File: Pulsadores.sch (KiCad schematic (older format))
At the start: 13 parts, among them SW1 Izquierda, SW2 Arriba, SW3 Abajo, SW4 Derecha, U6 74HC148

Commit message: añaadido zocalo para sensor de temperatura y primera distribucion sobre la PCB
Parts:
- added C7: 100n, Capacitors_SMD:C_0805, symbol C
- R21, R22, R23, R24, R25, R26, R27, R28: footprint (none) -> Resistors_SMD:R_0805
- SW1, SW2, SW3, SW4: footprint (none) -> Relays_and_Contacts:CANAL_ELECTRONIC_DTSM-31N-B
- U6: footprint (none) -> Housings_SOIC:SOIC-16_3.9x9.9mm_Pitch1.27mm
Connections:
- net +5V: now also C7.1
- net GND: now also C7.2
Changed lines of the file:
@@
 $Descr User 8268 5846
 encoding utf-8
-Sheet 9 13
+Sheet 9 14
 Title ""
 Date ""
@@
 F 0 "U6" H 5650 3075 50  0000 C CNN
 F 1 "74HC148" H 5650 2984 50  0000 C CNN
-F 2 "" H 5650 2450 50  0000 C CNN
+F 2 "Housings_SOIC:SOIC-16_3.9x9.9mm_Pitch1.27mm" H 5650 2450 50  0001 C CNN
 F 3 "http://www.tme.eu/es/Document/f2fc394d57399d0b6e6c6b1f0163be7e/SN74HC148N.pdf" H 5650 2450 50  0001 C CNN
 F 4 "Texas Instruments" H 5650 2450 60  0001 C CNN "Fabricante"
@@
 F 0 "SW2" H 2400 2305 50  0000 C CNN
 F 1 "Arriba" H 2400 2214 50  0000 C CNN
-F 2 "" H 2400 2050 50  0000 C CNN
+F 2 "Relays_and_Contacts:CANAL_ELECTRONIC_DTSM-31N-B" H 2400 2050 50  0001 C CNN
 F 3 "" H 2400 2050 50  0000 C CNN
 	1    2400 2050
@@
 F 0 "SW3" H 2400 3355 50  0000 C CNN
 F 1 "Abajo" H 2400 3264 50  0000 C CNN
-F 2 "" H 2400 3100 50  0000 C CNN
+F 2 "Relays_and_Contacts:CANAL_ELECTRONIC_DTSM-31N-B" H 2400 3100 50  0001 C CNN
 F 3 "" H 2400 3100 50  0000 C CNN
 	1    2400 3100
@@
 F 0 "SW4" H 3250 2855 50  0000 C CNN
 F 1 "Derecha" H 3250 2764 50  0000 C CNN
-F 2 "" H 3250 2600 50  0000 C CNN
+F 2 "Relays_and_Contacts:CANAL_ELECTRONIC_DTSM-31N-B" H 3250 2600 50  0001 C CNN
 F 3 "" H 3250 2600 50  0000 C CNN
 	1    3250 2600
@@
 F 0 "SW1" H 1450 2855 50  0000 C CNN
 F 1 "Izquierda" H 1450 2764 50  0000 C CNN
-F 2 "" H 1450 2600 50  0000 C CNN
+F 2 "Relays_and_Contacts:CANAL_ELECTRONIC_DTSM-31N-B" H 1450 2600 50  0001 C CNN
 F 3 "" H 1450 2600 50  0000 C CNN
 	1    1450 2600
@@
 $EndComp
 Wire Wire Line
-	2700 2050 3950 2050
-Wire Wire Line
-	3950 2050 5050 2050
-Wire Wire Line
-	2700 2150 4200 2150
-Wire Wire Line
-	4200 2150 5050 2150
+	2700 2050 5050 2050
+Wire Wire Line
+	2700 2150 5050 2150
 Wire Wire Line
 	2700 2150 2700 2600
@@
 	3650 2600 3650 2250
 Wire Wire Line
-	3650 2250 4450 2250
-Wire Wire Line
-	4450 2250 5050 2250
-Wire Wire Line
-	3750 2350 4700 2350
-Wire Wire Line
-	4700 2350 5050 2350
+	3650 2250 5050 2250
+Wire Wire Line
+	3750 2350 5050 2350
 Wire Wire Line
 	3750 3100 3750 2350
@@
 F 0 "R21" H 4020 1696 50  0000 L CNN
 F 1 "10K" V 3950 1550 50  0000 L CNN
-F 2 "" V 3880 1650 50  0000 C CNN
+F 2 "Resistors_SMD:R_0805" V 3880 1650 50  0001 C CNN
 F 3 "" H 3950 1650 50  0000 C CNN
 F 4 "~" H 3950 1650 60  0001 C CNN "Fabricante"
@@
 F 0 "R23" H 4270 1696 50  0000 L CNN
 F 1 "10K" V 4200 1550 50  0000 L CNN
-F 2 "" V 4130 1650 50  0000 C CNN
+F 2 "Resistors_SMD:R_0805" V 4130 1650 50  0001 C CNN
 F 3 "" H 4200 1650 50  0000 C CNN
 F 4 "~" H 4200 1650 60  0001 C CNN "Fabricante"
@@
 F 0 "R25" H 4520 1696 50  0000 L CNN
 F 1 "10K" V 4450 1550 50  0000 L CNN
-F 2 "" V 4380 1650 50  0000 C CNN
+F 2 "Resistors_SMD:R_0805" V 4380 1650 50  0001 C CNN
 F 3 "" H 4450 1650 50  0000 C CNN
 F 4 "~" H 4450 1650 60  0001 C CNN "Fabricante"
@@
 F 0 "R27" H 4770 1696 50  0000 L CNN
 F 1 "10K" V 4700 1550 50  0000 L CNN
-F 2 "" V 4630 1650 50  0000 C CNN
+F 2 "Resistors_SMD:R_0805" V 4630 1650 50  0001 C CNN
 F 3 "" H 4700 1650 50  0000 C CNN
 F 4 "~" H 4700 1650 60  0001 C CNN "Fabricante"
@@
 A0
 Wire Wire Line
-	6550 2250 6550 2250
-Wire Wire Line
-	6550 2250 6700 2250
+	6250 2250 6700 2250
 Text GLabel 6700 2250 2    60   Output ~ 0
 A1
-Wire Wire Line
-	6250 2250 6550 2250
 NoConn ~ 6250 2350
 $Comp
@@
 F 0 "R22" H 4020 3346 50  0000 L CNN
 F 1 "10K" V 3950 3200 50  0000 L CNN
-F 2 "" V 3880 3300 50  0000 C CNN
+F 2 "Resistors_SMD:R_0805" V 3880 3300 50  0001 C CNN
 F 3 "" H 3950 3300 50  0000 C CNN
 F 4 "~" H 3950 3300 60  0001 C CNN "Fabricante"
@@
 F 0 "R24" H 4270 3346 50  0000 L CNN
 F 1 "10K" V 4200 3200 50  0000 L CNN
-F 2 "" V 4130 3300 50  0000 C CNN
+F 2 "Resistors_SMD:R_0805" V 4130 3300 50  0001 C CNN
 F 3 "" H 4200 3300 50  0000 C CNN
 F 4 "~" H 4200 3300 60  0001 C CNN "Fabricante"
@@
 F 0 "R26" H 4520 3346 50  0000 L CNN
 F 1 "10K" V 4450 3200 50  0000 L CNN
-F 2 "" V 4380 3300 50  0000 C CNN
+F 2 "Resistors_SMD:R_0805" V 4380 3300 50  0001 C CNN
 F 3 "" H 4450 3300 50  0000 C CNN
 F 4 "~" H 4450 3300 60  0001 C CNN "Fabricante"
@@
 F 0 "R28" H 4770 3346 50  0000 L CNN
 F 1 "10K" V 4700 3200 50  0000 L CNN
-F 2 "" V 4630 3300 50  0000 C CNN
+F 2 "Resistors_SMD:R_0805" V 4630 3300 50  0001 C CNN
 F 3 "" H 4700 3300 50  0000 C CNN
 F 4 "~" H 4700 3300 60  0001 C CNN "Fabricante"
@@
 	1    0    0    -1
 $EndComp
+$Comp
+L C C7
+U 1 1 57993D3A
+P 6450 1350
+F 0 "C7" H 6475 1450 50  0000 L CNN
+F 1 "100n" H 6475 1250 50  0000 L CNN
+F 2 "Capacitors_SMD:C_0805" H 6488 1200 50  0001 C CNN
+F 3 "" H 6450 1350 50  0000 C CNN
+F 4 "~" H 6450 1350 60  0001 C CNN "Fabricante"
+F 5 "~" H 6450 1350 60  0001 C CNN "Ref"
+F 6 "~" H 6450 1350 60  0001 C CNN "Potencia"
+F 7 "~" H 6450 1350 60  0001 C CNN "Tolerancia"
+F 8 "~" H 6450 1350 60  0001 C CNN "Provedor"
+F 9 "~" H 6450 1350 60  0001 C CNN "Ref_Proveedor"
+	1    6450 1350
+	1    0    0    -1
+$EndComp
+$Comp
+L GND #PWR037
+U 1 1 57993D41
+P 6450 1600
+F 0 "#PWR037" H 6450 1350 50  0001 C CNN
+F 1 "GND" H 6450 1450 50  0000 C CNN
+F 2 "" H 6450 1600 50  0000 C CNN
+F 3 "" H 6450 1600 50  0000 C CNN
+	1    6450 1600
+	1    0    0    -1
+$EndComp
+$Comp
+L +5V #PWR038
+U 1 1 57993D47
+P 6450 1050
+F 0 "#PWR038" H 6450 900 50  0001 C CNN
+F 1 "+5V" H 6450 1190 50  0000 C CNN
+F 2 "" H 6450 1050 50  0000 C CNN
+F 3 "" H 6450 1050 50  0000 C CNN
+	1    6450 1050
+	1    0    0    -1
+$EndComp
+Wire Wire Line
+	6450 1200 6450 1050
+Wire Wire Line
+	6450 1600 6450 1500
 $EndSCHEMATC

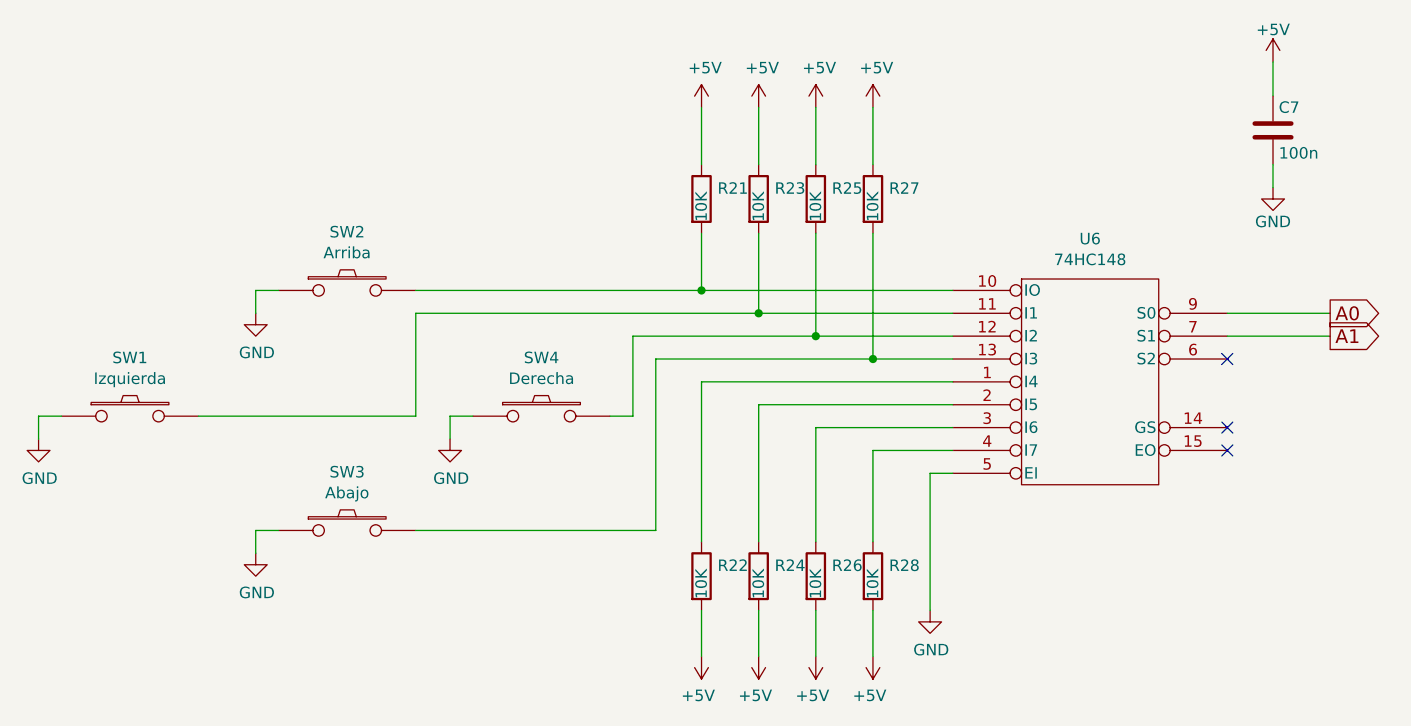
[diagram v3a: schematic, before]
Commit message: ordenar referencias de componentes
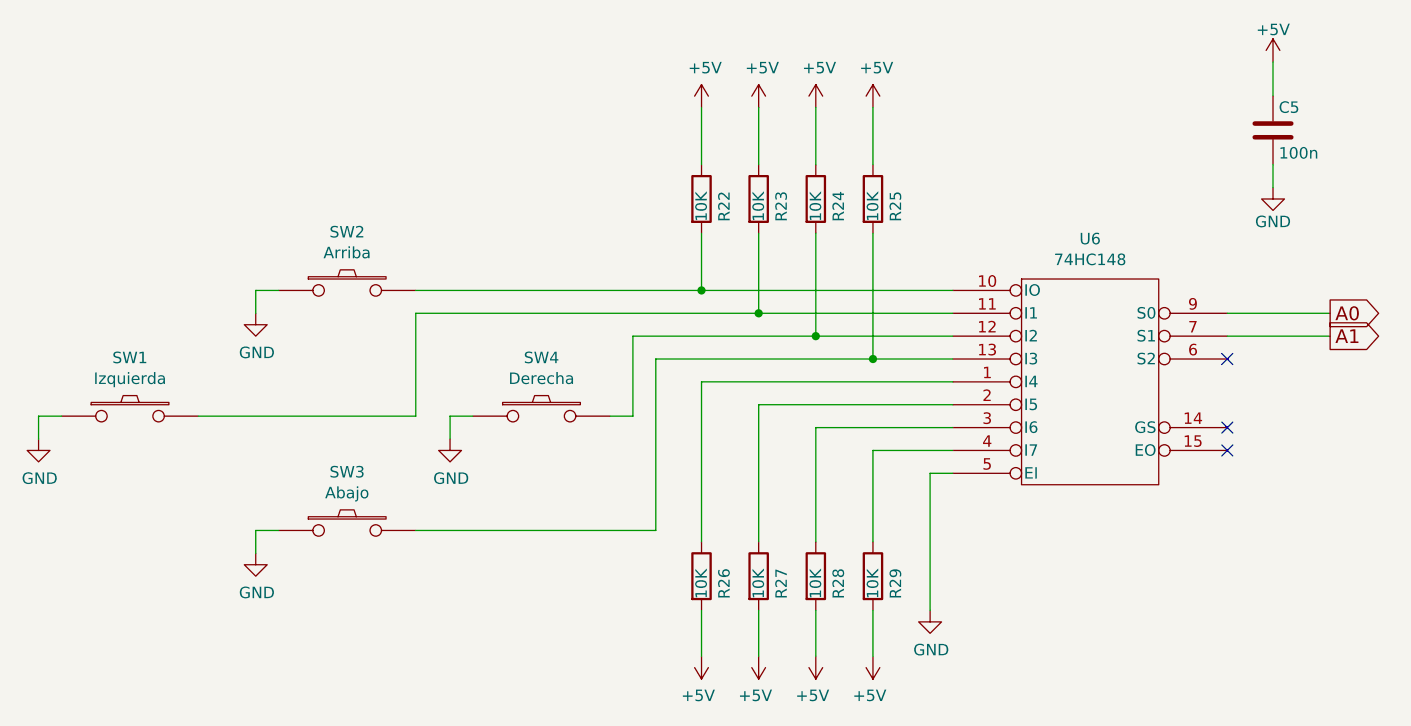
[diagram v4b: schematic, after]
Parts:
- C5: renamed from C7; Fabricante (none) -> SAMSUNG; Provedor (none) -> TME; Ref (none) -> CL21B104KBCNNNC; Ref_Proveedor (none) -> CL21B104KBCNNNC
- R22: renamed from R21; Fabricante (none) -> VISHAY; Potencia (none) -> 1/8W; Provedor (none) -> TME; Ref (none) -> CRCW080510K0FKEA; Ref_Proveedor (none) -> CRCW080510K0FKEA; Tolerancia (none) -> 1%
- R23: Fabricante (none) -> VISHAY; Potencia (none) -> 1/8W; Provedor (none) -> TME; Ref (none) -> CRCW080510K0FKEA; Ref_Proveedor (none) -> CRCW080510K0FKEA; Tolerancia (none) -> 1%
- R24: renamed from R25; Fabricante (none) -> VISHAY; Potencia (none) -> 1/8W; Provedor (none) -> TME; Ref (none) -> CRCW080510K0FKEA; Ref_Proveedor (none) -> CRCW080510K0FKEA; Tolerancia (none) -> 1%
- R25: renamed from R27; Fabricante (none) -> VISHAY; Potencia (none) -> 1/8W; Provedor (none) -> TME; Ref (none) -> CRCW080510K0FKEA; Ref_Proveedor (none) -> CRCW080510K0FKEA; Tolerancia (none) -> 1%
- R26: renamed from R22; Fabricante (none) -> VISHAY; Potencia (none) -> 1/8W; Provedor (none) -> TME; Ref (none) -> CRCW080510K0FKEA; Ref_Proveedor (none) -> CRCW080510K0FKEA; Tolerancia (none) -> 1%
- R27: renamed from R24; Fabricante (none) -> VISHAY; Potencia (none) -> 1/8W; Provedor (none) -> TME; Ref (none) -> CRCW080510K0FKEA; Ref_Proveedor (none) -> CRCW080510K0FKEA; Tolerancia (none) -> 1%
- R28: renamed from R26; Fabricante (none) -> VISHAY; Potencia (none) -> 1/8W; Provedor (none) -> TME; Ref (none) -> CRCW080510K0FKEA; Ref_Proveedor (none) -> CRCW080510K0FKEA; Tolerancia (none) -> 1%
- R29: renamed from R28; Fabricante (none) -> VISHAY; Potencia (none) -> 1/8W; Provedor (none) -> TME; Ref (none) -> CRCW080510K0FKEA; Ref_Proveedor (none) -> CRCW080510K0FKEA; Tolerancia (none) -> 1%
- SW1, SW2, SW3, SW4: Fabricante (none) -> CANAL ELECTRONIC; Provedor (none) -> TME; Ref (none) -> SN74HC148D; Ref_Proveedor (none) -> DTSM-31N-B
- U6: Provedor SN74HC148D -> TME

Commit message: cambiados encoder y potenciometro
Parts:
- R22, R23, R24, R25, R26, R27, R28, R29: footprint Resistors_SMD:R_0805 -> Resistencias:R_0805
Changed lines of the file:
@@
 	1050 2600 1050 2700
 $Comp
-L GND #PWR28
+L GND #PWR030
 U 1 1 57951274
 P 1050 2700
-F 0 "#PWR28" H 1050 2450 50  0001 C CNN
+F 0 "#PWR030" H 1050 2450 50  0001 C CNN
 F 1 "GND" H 1055 2527 50  0000 C CNN
 F 2 "" H 1050 2700 50  0000 C CNN
@@
 	2000 3100 2000 3200
 $Comp
-L GND #PWR30
+L GND #PWR031
 U 1 1 579512A4
 P 2000 3200
-F 0 "#PWR30" H 2000 2950 50  0001 C CNN
+F 0 "#PWR031" H 2000 2950 50  0001 C CNN
 F 1 "GND" H 2005 3027 50  0000 C CNN
 F 2 "" H 2000 3200 50  0000 C CNN
@@
 	2000 2050 2000 2150
 $Comp
-L GND #PWR29
+L GND #PWR032
 U 1 1 579512CF
 P 2000 2150
-F 0 "#PWR29" H 2000 1900 50  0001 C CNN
+F 0 "#PWR032" H 2000 1900 50  0001 C CNN
 F 1 "GND" H 2005 1977 50  0000 C CNN
 F 2 "" H 2000 2150 50  0000 C CNN
@@
 	2850 2600 2850 2700
 $Comp
-L GND #PWR31
+L GND #PWR033
 U 1 1 5795130B
 P 2850 2700
-F 0 "#PWR31" H 2850 2450 50  0001 C CNN
+F 0 "#PWR033" H 2850 2450 50  0001 C CNN
 F 1 "GND" H 2855 2527 50  0000 C CNN
 F 2 "" H 2850 2700 50  0000 C CNN
@@
 F 0 "R22" V 4050 1550 50  0000 L CNN
 F 1 "10K" V 3950 1550 50  0000 L CNN
-F 2 "Resistors_SMD:R_0805" V 3880 1650 50  0001 C CNN
+F 2 "Resistencias:R_0805" V 3880 1650 50  0001 C CNN
 F 3 "" H 3950 1650 50  0000 C CNN
 F 4 "VISHAY" H 3950 1650 60  0001 C CNN "Fabricante"
@@
 F 0 "R23" V 4300 1550 50  0000 L CNN
 F 1 "10K" V 4200 1550 50  0000 L CNN
-F 2 "Resistors_SMD:R_0805" V 4130 1650 50  0001 C CNN
+F 2 "Resistencias:R_0805" V 4130 1650 50  0001 C CNN
 F 3 "" H 4200 1650 50  0000 C CNN
 F 4 "VISHAY" H 3950 1650 60  0001 C CNN "Fabricante"
@@
 F 0 "R24" V 4550 1550 50  0000 L CNN
 F 1 "10K" V 4450 1550 50  0000 L CNN
-F 2 "Resistors_SMD:R_0805" V 4380 1650 50  0001 C CNN
+F 2 "Resistencias:R_0805" V 4380 1650 50  0001 C CNN
 F 3 "" H 4450 1650 50  0000 C CNN
 F 4 "VISHAY" H 3950 1650 60  0001 C CNN "Fabricante"
@@
 F 0 "R25" V 4800 1550 50  0000 L CNN
 F 1 "10K" V 4700 1550 50  0000 L CNN
-F 2 "Resistors_SMD:R_0805" V 4630 1650 50  0001 C CNN
+F 2 "Resistencias:R_0805" V 4630 1650 50  0001 C CNN
 F 3 "" H 4700 1650 50  0000 C CNN
 F 4 "VISHAY" H 3950 1650 60  0001 C CNN "Fabricante"
@@
 	3950 1500 3950 1250
 $Comp
-L +5V #PWR32
+L +5V #PWR034
 U 1 1 5795193F
 P 3950 1250
-F 0 "#PWR32" H 3950 1100 50  0001 C CNN
+F 0 "#PWR034" H 3950 1100 50  0001 C CNN
 F 1 "+5V" H 3965 1423 50  0000 C CNN
 F 2 "" H 3950 1250 50  0000 C CNN
@@
 $EndComp
 $Comp
-L +5V #PWR34
+L +5V #PWR035
 U 1 1 5795196C
 P 4200 1250
-F 0 "#PWR34" H 4200 1100 50  0001 C CNN
+F 0 "#PWR035" H 4200 1100 50  0001 C CNN
 F 1 "+5V" H 4215 1423 50  0000 C CNN
 F 2 "" H 4200 1250 50  0000 C CNN
@@
 $EndComp
 $Comp
-L +5V #PWR36
+L +5V #PWR036
 U 1 1 57951992
 P 4450 1250
-F 0 "#PWR36" H 4450 1100 50  0001 C CNN
+F 0 "#PWR036" H 4450 1100 50  0001 C CNN
 F 1 "+5V" H 4465 1423 50  0000 C CNN
 F 2 "" H 4450 1250 50  0000 C CNN
@@
 $EndComp
 $Comp
-L +5V #PWR38
+L +5V #PWR037
 U 1 1 579519B8
 P 4700 1250
-F 0 "#PWR38" H 4700 1100 50  0001 C CNN
+F 0 "#PWR037" H 4700 1100 50  0001 C CNN
 F 1 "+5V" H 4715 1423 50  0000 C CNN
 F 2 "" H 4700 1250 50  0000 C CNN
@@
 F 0 "R26" V 4050 3200 50  0000 L CNN
 F 1 "10K" V 3950 3200 50  0000 L CNN
-F 2 "Resistors_SMD:R_0805" V 3880 3300 50  0001 C CNN
+F 2 "Resistencias:R_0805" V 3880 3300 50  0001 C CNN
 F 3 "" H 3950 3300 50  0000 C CNN
 F 4 "VISHAY" H 3950 1650 60  0001 C CNN "Fabricante"
@@
 F 0 "R27" V 4300 3200 50  0000 L CNN
 F 1 "10K" V 4200 3200 50  0000 L CNN
-F 2 "Resistors_SMD:R_0805" V 4130 3300 50  0001 C CNN
+F 2 "Resistencias:R_0805" V 4130 3300 50  0001 C CNN
 F 3 "" H 4200 3300 50  0000 C CNN
 F 4 "VISHAY" H 3950 1650 60  0001 C CNN "Fabricante"
@@
 F 0 "R28" V 4550 3200 50  0000 L CNN
 F 1 "10K" V 4450 3200 50  0000 L CNN
-F 2 "Resistors_SMD:R_0805" V 4380 3300 50  0001 C CNN
+F 2 "Resistencias:R_0805" V 4380 3300 50  0001 C CNN
 F 3 "" H 4450 3300 50  0000 C CNN
 F 4 "VISHAY" H 3950 1650 60  0001 C CNN "Fabricante"
@@
 F 0 "R29" V 4800 3200 50  0000 L CNN
 F 1 "10K" V 4700 3200 50  0000 L CNN
-F 2 "Resistors_SMD:R_0805" V 4630 3300 50  0001 C CNN
+F 2 "Resistencias:R_0805" V 4630 3300 50  0001 C CNN
 F 3 "" H 4700 3300 50  0000 C CNN
 F 4 "VISHAY" H 3950 1650 60  0001 C CNN "Fabricante"
@@
 	3950 3450 3950 3650
 $Comp
-L +5V #PWR33
+L +5V #PWR038
 U 1 1 579524C5
 P 3950 3650
-F 0 "#PWR33" H 3950 3500 50  0001 C CNN
+F 0 "#PWR038" H 3950 3500 50  0001 C CNN
 F 1 "+5V" H 3965 3823 50  0000 C CNN
 F 2 "" H 3950 3650 50  0000 C CNN
@@
 $EndComp
 $Comp
-L +5V #PWR35
+L +5V #PWR039
 U 1 1 57952518
 P 4200 3650
-F 0 "#PWR35" H 4200 3500 50  0001 C CNN
+F 0 "#PWR039" H 4200 3500 50  0001 C CNN
 F 1 "+5V" H 4215 3823 50  0000 C CNN
 F 2 "" H 4200 3650 50  0000 C CNN
@@
 $EndComp
 $Comp
-L +5V #PWR37
+L +5V #PWR040
 U 1 1 5795254A
 P 4450 3650
-F 0 "#PWR37" H 4450 3500 50  0001 C CNN
+F 0 "#PWR040" H 4450 3500 50  0001 C CNN
 F 1 "+5V" H 4465 3823 50  0000 C CNN
 F 2 "" H 4450 3650 50  0000 C CNN
@@
 $EndComp
 $Comp
-L +5V #PWR39
+L +5V #PWR041
 U 1 1 5795257C
 P 4700 3650
-F 0 "#PWR39" H 4700 3500 50  0001 C CNN
+F 0 "#PWR041" H 4700 3500 50  0001 C CNN
 F 1 "+5V" H 4715 3823 50  0000 C CNN
 F 2 "" H 4700 3650 50  0000 C CNN
@@
 	4950 2850 4950 3450
 $Comp
-L GND #PWR40
+L GND #PWR042
 U 1 1 5795449C
 P 4950 3450
-F 0 "#PWR40" H 4950 3200 50  0001 C CNN
+F 0 "#PWR042" H 4950 3200 50  0001 C CNN
 F 1 "GND" H 4955 3277 50  0000 C CNN
 F 2 "" H 4950 3450 50  0000 C CNN
@@
 $EndComp
 $Comp
-L GND #PWR42
+L GND #PWR043
 U 1 1 57993D41
 P 6450 1600
-F 0 "#PWR42" H 6450 1350 50  0001 C CNN
+F 0 "#PWR043" H 6450 1350 50  0001 C CNN
 F 1 "GND" H 6450 1450 50  0000 C CNN
 F 2 "" H 6450 1600 50  0000 C CNN
@@
 $EndComp
 $Comp
-L +5V #PWR41
+L +5V #PWR044
 U 1 1 57993D47
 P 6450 1050
-F 0 "#PWR41" H 6450 900 50  0001 C CNN
+F 0 "#PWR044" H 6450 900 50  0001 C CNN
 F 1 "+5V" H 6450 1190 50  0000 C CNN
 F 2 "" H 6450 1050 50  0000 C CNN
